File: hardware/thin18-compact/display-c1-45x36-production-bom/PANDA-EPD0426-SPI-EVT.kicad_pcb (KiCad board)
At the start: 2 copper layers, 45 x 36 mm, 37 parts, among them J1 DF40C-60DP-0.4V(51), J2 FH12-24S-0.5SH(55), Q1 NX3008NBK,215, U1 AIP74LVC2G17GC363.TR, U2 AIP74LVC2G17GC363.TR, U3 AIP74LVC2G17GC363.TR

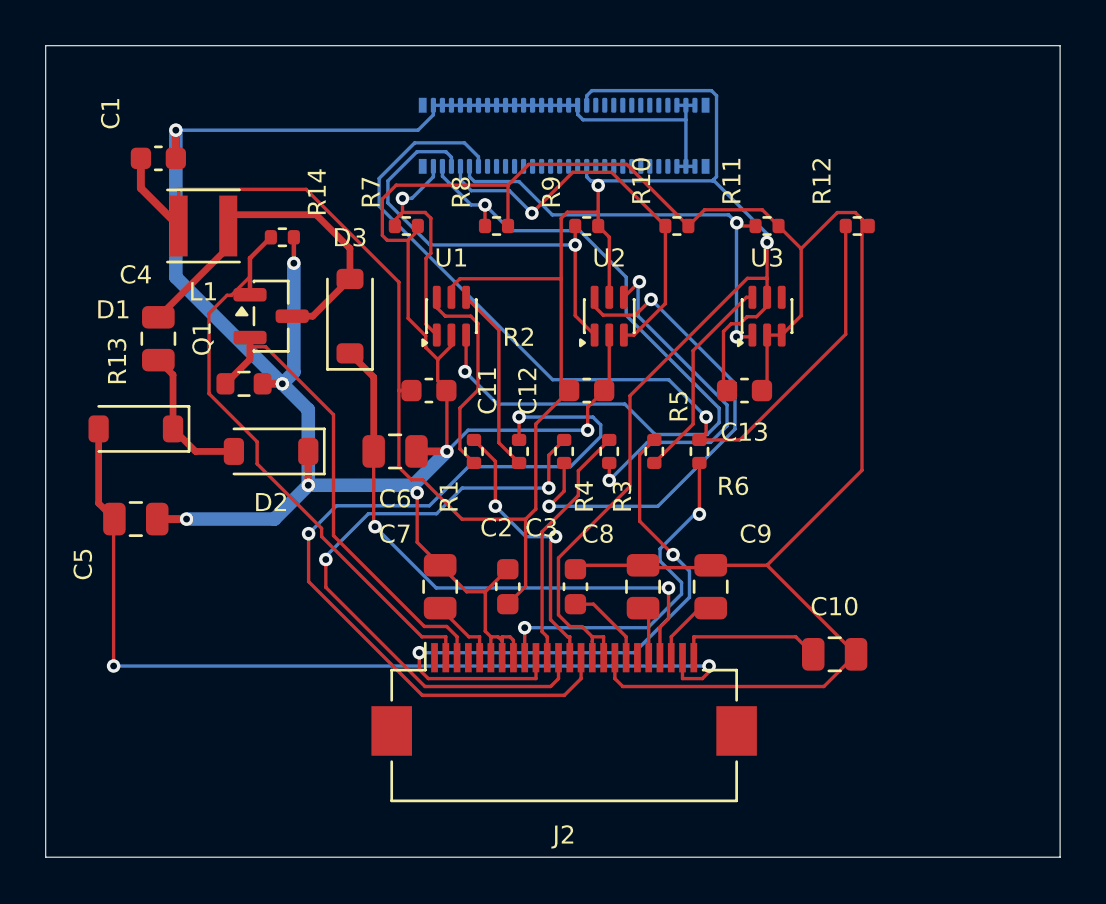
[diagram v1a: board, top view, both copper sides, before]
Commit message: hw: correct prototype footprints and prepare Split-C1 JLC CAM handoff
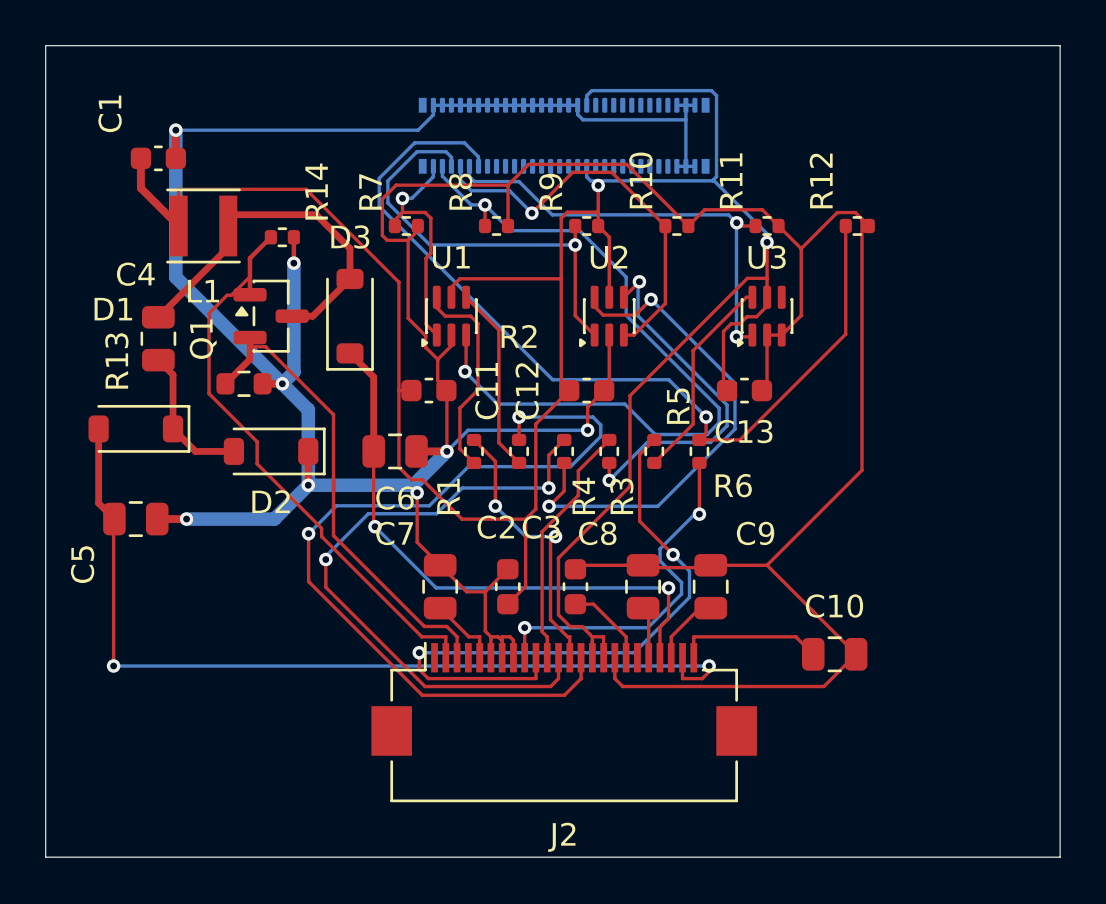
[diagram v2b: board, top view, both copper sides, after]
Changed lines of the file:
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@@
 			(effects
 				(font
-					(size 0.8 0.8)
-					(thickness 0.1)
+					(size 1 1)
+					(thickness 0.15)
 				)
 			)
@@
 			(effects
 				(font
-					(size 0.8 0.8)
-					(thickness 0.1)
+					(size 1 1)
+					(thickness 0.15)
 				)
 			)
@@
 			(effects
 				(font
-					(size 0.8 0.8)
-					(thickness 0.1)
+					(size 1 1)
+					(thickness 0.15)
 				)
 			)
@@
 			(effects
 				(font
-					(size 0.8 0.8)
-					(thickness 0.1)
+					(size 1 1)
+					(thickness 0.15)
 				)
 			)
@@
 			(effects
 				(font
-					(size 0.8 0.8)
-					(thickness 0.1)
+					(size 1 1)
+					(thickness 0.15)
 				)
 			)
@@
 			(effects
 				(font
-					(size 0.8 0.8)
-					(thickness 0.1)
+					(size 1 1)
+					(thickness 0.15)
 				)
 			)
@@
 			(effects
 				(font
-					(size 0.8 0.8)
-					(thickness 0.1)
+					(size 1 1)
+					(thickness 0.15)
 				)
 			)
@@
 			(effects
 				(font
-					(size 0.8 0.8)
-					(thickness 0.1)
+					(size 1 1)
+					(thickness 0.15)
 				)
 			)
@@
 			(effects
 				(font
-					(size 0.8 0.8)
-					(thickness 0.1)
+					(size 1 1)
+					(thickness 0.15)
 				)
 			)
@@
 			(effects
 				(font
-					(size 0.8 0.8)
-					(thickness 0.1)
+					(size 1 1)
+					(thickness 0.15)
 				)
 			)
@@
 			(effects
 				(font
-					(size 0.8 0.8)
-					(thickness 0.1)
+					(size 1 1)
+					(thickness 0.15)
 				)
 			)
@@
 			(effects
 				(font
-					(size 0.8 0.8)
-					(thickness 0.1)
+					(size 1 1)
+					(thickness 0.15)
 				)
 			)
@@
 			(effects
 				(font
-					(size 0.8 0.8)
-					(thickness 0.1)
+					(size 1 1)
+					(thickness 0.15)
 				)
 			)
@@
 			(effects
 				(font
-					(size 0.8 0.8)
-					(thickness 0.1)
+					(size 1 1)
+					(thickness 0.15)
 				)
 			)
@@
 			(effects
 				(font
-					(size 0.8 0.8)
-					(thickness 0.1)
+					(size 1 1)
+					(thickness 0.15)
 				)
 			)
@@
 			(effects
 				(font
-					(size 0.8 0.8)
-					(thickness 0.1)
+					(size 1 1)
+					(thickness 0.15)
 				)
 			)
@@
 			(effects
 				(font
-					(size 0.8 0.8)
-					(thickness 0.1)
+					(size 1 1)
+					(thickness 0.15)
 				)
 			)
@@
 			(effects
 				(font
-					(size 0.8 0.8)
-					(thickness 0.1)
+					(size 1 1)
+					(thickness 0.15)
 				)
 			)
@@
 			(effects
 				(font
-					(size 0.8 0.8)
-					(thickness 0.1)
+					(size 1 1)
+					(thickness 0.15)
 				)
 			)
@@
 			(effects
 				(font
-					(size 0.8 0.8)
-					(thickness 0.1)
+					(size 1 1)
+					(thickness 0.15)
 				)
 			)
@@
 			(effects
 				(font
-					(size 0.8 0.8)
-					(thickness 0.1)
+					(size 1 1)
+					(thickness 0.15)
 				)
 			)
@@
 			(effects
 				(font
-					(size 0.8 0.8)
-					(thickness 0.1)
+					(size 1 1)
+					(thickness 0.15)
 				)
 			)
@@
 			(effects
 				(font
-					(size 0.8 0.8)
-					(thickness 0.1)
+					(size 1 1)
+					(thickness 0.15)
 				)
 			)
@@
 			(effects
 				(font
-					(size 0.8 0.8)
-					(thickness 0.1)
+					(size 1 1)
+					(thickness 0.15)
 				)
 			)
@@
 			(effects
 				(font
-					(size 0.8 0.8)
-					(thickness 0.1)
+					(size 1 1)
+					(thickness 0.15)
 				)
 			)
@@
 			(effects
 				(font
-					(size 0.8 0.8)
-					(thickness 0.1)
+					(size 1 1)
+					(thickness 0.15)
 				)
 			)
@@
 			(effects
 				(font
-					(size 0.8 0.8)
-					(thickness 0.1)
+					(size 1 1)
+					(thickness 0.15)
 				)
 			)
@@
 			(effects
 				(font
-					(size 0.8 0.8)
-					(thickness 0.1)
+					(size 1 1)
+					(thickness 0.15)
 				)
 			)
@@
 			(effects
 				(font
-					(size 0.8 0.8)
-					(thickness 0.1)
+					(size 1 1)
+					(thickness 0.15)
 				)
 			)
@@
 			(effects
 				(font
-					(size 0.8 0.8)
-					(thickness 0.1)
+					(size 1 1)
+					(thickness 0.15)
 				)
 			)
@@
 			(effects
 				(font
-					(size 0.8 0.8)
-					(thickness 0.1)
+					(size 1 1)
+					(thickness 0.15)
 				)
 			)
@@
 			(effects
 				(font
-					(size 0.8 0.8)
-					(thickness 0.1)
+					(size 1 1)
+					(thickness 0.15)
 				)
 			)
@@
 			(effects
 				(font
-					(size 0.8 0.8)
-					(thickness 0.1)
+					(size 1 1)
+					(thickness 0.15)
 				)
 			)
@@
 			(effects
 				(font
-					(size 0.8 0.8)
-					(thickness 0.1)
+					(size 1 1)
+					(thickness 0.15)
 				)
 			)
@@
 			(effects
 				(font
-					(size 0.8 0.8)
-					(thickness 0.1)
+					(size 1 1)
+					(thickness 0.15)
 				)
 			)
@@
 			(effects
 				(font
-					(size 0.8 0.8)
-					(thickness 0.1)
+					(size 1 1)
+					(thickness 0.15)
 				)
 			)
@@
 			(effects
 				(font
-					(size 0.8 0.8)
-					(thickness 0.1)
+					(size 1 1)
+					(thickness 0.15)
 				)
 				(justify mirror)

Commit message: hw: apply reviewed domestic ECOs and gate incomplete Split-C1 orders
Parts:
- C4, C5, C6, C7, C8, C9: value 4.7u 25V X5R -> 4.7u 25V X7R
- D1, D2, D3: value MBR0530T1G -> MBR0530; footprint Diode_SMD:D_SOD-123 -> panda-r6-display:MBR0530_JSCJ_SOD123
- J1: value DF40C-60DP-0.4V(51) -> HC-PBB40C-60DP-0.4V-02; footprint Connector_Hirose_DF40:Hirose_DF40C-60DP-0.4V_2x30-1MP_P0.4mm -> panda-r6-display:HCTL_PBB40C_60DP_04V

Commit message: hw: apply domestic wire, FPC and inductor ECOs with replay guards
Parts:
- L1: value 47u 0.25A -> 47uH / Sunlord; footprint panda-r6-display:L_Taiyo_NRH3010_3030 -> panda-r6-display:Sunlord_SWPA3012_47u
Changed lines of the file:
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@@
 		)
 	)
-	(footprint "panda-r6-display:L_Taiyo_NRH3010_3030"
+	(footprint "panda-r6-display:Sunlord_SWPA3012_47u"
 		(layer "F.Cu")
 		(at 7 8)
-		(descr "Taiyo Yuden NRH3010 / LSXNE3030KK, 3.0x3.0mm maxH1.0mm. Catalog NR30 recommended land A0.8/Bcentre2.2/C2.7; supplier footprint review pending.")
+		(descr "Sunlord SWPA3012S manufacturer land pattern; original series drawing reviewed; Fab uses maximum body XY and no foreign 3D model.")
 		(property "Reference" "L1"
 			(at 0 2.924999 0)
@@
 			)
 		)
-		(property "Value" "47u 0.25A"
+		(property "Value" "47uH / Sunlord"
 			(at 0 2.4 0)
 			(layer "F.Fab")
@@
 			)
 		)
-		(property "Datasheet" "https://www.yuden.co.jp/"
-			(at 0 0 0)
-			(layer "F.Fab")
-			(hide yes)
-			(effects
-				(font
-					(size 1.27 1.27)
-				)
-			)
-		)(property "Manufacturer" "Taiyo Yuden" (at 0 0 0) (layer "F.Fab") (hide yes) (effects (font (size 1 1))))
-		(property "Description" ""
+		(property "Datasheet" "https://atta.szlcsc.com/upload/public/pdf/source/20241120/5FB31A17AAA509171003FB8365AF70A5.pdf"
 			(at 0 0 0)
 			(layer "F.Fab")
@@
 			)
 		)
-		(property "MPN" "LSXNE3030KKT470MN"
+(property "LCSC" ""
+			(at 0 0 0)
+			(layer "F.Fab")
+			(hide yes)
+			(effects
+				(font
+					(size 1.27 1.27)
+				)
+			)
+		)(property "Manufacturer" "Sunlord" (at 0 0 0) (layer "F.Fab") (hide yes) (effects (font (size 1 1))))
+		(property "Description" "47uH +/-20%,DCR1.885ohm max,Isat(Max/Typ).27/.35A,Irms(Max/Typ).35/.40A from original2024-06-19 p5; current headings retained, not claimed as guaranteed minimum. Body3.0+/-0.2mm square,max height1.2mm. p2 lands0.8x2.7mm,inner gap1.5mm,centers+/-1.15mm. Original maxDCR2.46ohm,height1.0mm,current.25A; boost peak/RESE corners, ripple, thermal and efficiency remain EVT. Taller by.2mm, mechanical budget updated. Exact supply/packing not yet accepted."
+			(at 0 0 0)
+			(layer "F.Fab")
+			(hide yes)
+			(effects
+				(font
+					(size 1.27 1.27)
+				)
+			)
+		)
+		(property "MPN" "SWPA3012S470MT"
 			(at 0 0 0)
 			(layer "F.SilkS")
@@
 		(attr smd)
 		(duplicate_pad_numbers_are_jumpers no)
-		(fp_line
-			(start -1.6 -1.6)
-			(end 1.6 -1.6)
-			(stroke
-				(width 0.12)
-				(type default)
-			)
-			(layer "F.SilkS")
-		)
-		(fp_line
-			(start -1.6 1.6)
-			(end 1.6 1.6)
-			(stroke
-				(width 0.12)
-				(type default)
-			)
-			(layer "F.SilkS")
-		)
-		(fp_rect
-			(start -1.8 -1.8)
-			(end 1.8 1.8)
-			(stroke
-				(width 0.05)
-				(type default)
-			)
-			(fill no)
-			(layer "F.CrtYd")
-		)
-		(fp_rect
-			(start -1.5 -1.5)
-			(end 1.5 1.5)
-			(stroke
-				(width 0.1)
-				(type default)
-			)
-			(fill no)
-			(layer "F.Fab")
-		)
 		(pad "1" smd rect
-			(at -1.1 0)
+			(at -1.15 0)
 			(size 0.8 2.7)
 			(layers "F.Cu" "F.Mask" "F.Paste")
@@
 		)
 		(pad "2" smd rect
-			(at 1.1 0)
+			(at 1.15 0)
 			(size 0.8 2.7)
 			(layers "F.Cu" "F.Mask" "F.Paste")
@@
 		)
 		(embedded_fonts no)
-	)
+(fp_rect (start -1.6 -1.6) (end 1.6 1.6) (stroke (width 0.1) (type solid)) (fill no) (layer "F.Fab"))
+(fp_rect (start -1.85 -1.85) (end 1.85 1.85) (stroke (width 0.05) (type solid)) (fill no) (layer "F.CrtYd"))
+)
 	(footprint "Capacitor_SMD:C_0805_2012Metric"
 		(layer "F.Cu")

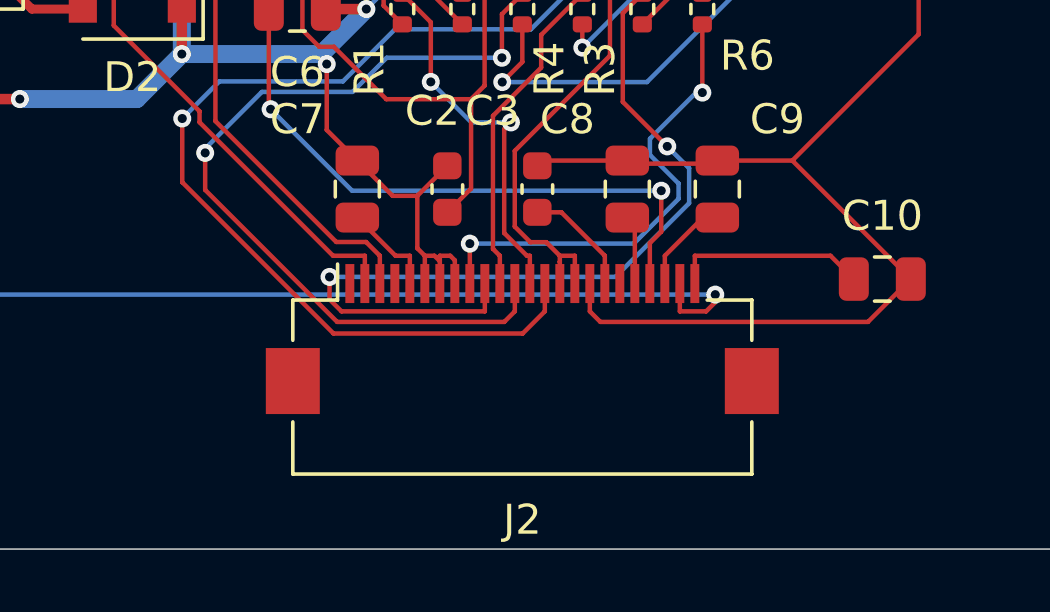
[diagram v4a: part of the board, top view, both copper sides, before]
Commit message: hardware: close three imported Split-C1 refs and two SMT maps
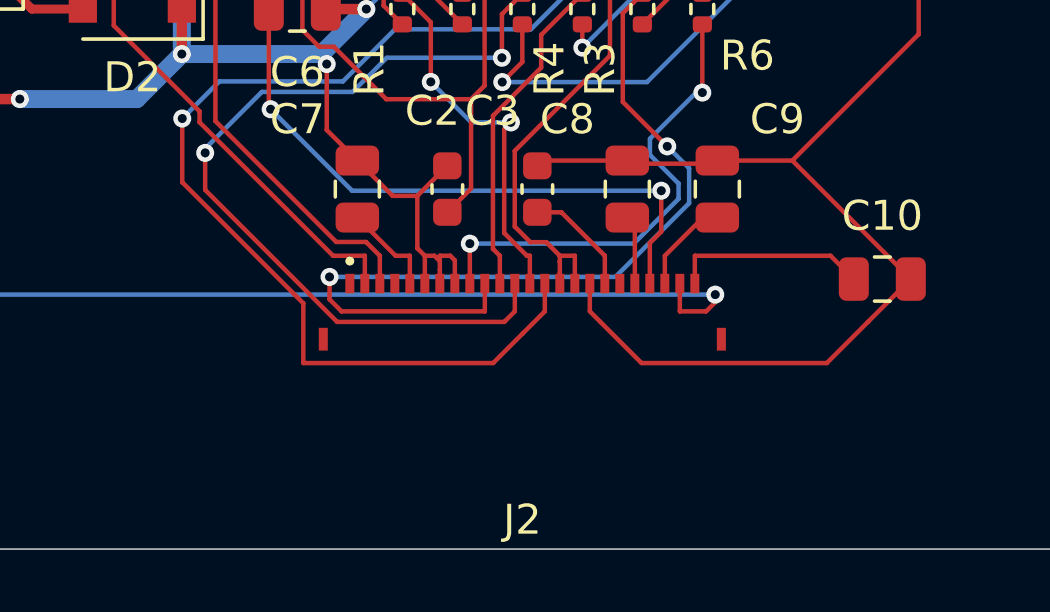
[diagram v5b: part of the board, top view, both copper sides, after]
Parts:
- J2: value FH12-24S-0.5SH(55) -> X05A10L24G; footprint Connector_FFC-FPC:Hirose_FH12-24S-0.5SH_1x24-1MP_P0.50mm_Horizontal -> panda-r6-display:XKB_X05A10L24G
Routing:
- net /MOSI: track 37.6 -> 39.6 mm
- net /GND: track 190.5 -> 191.6 mm

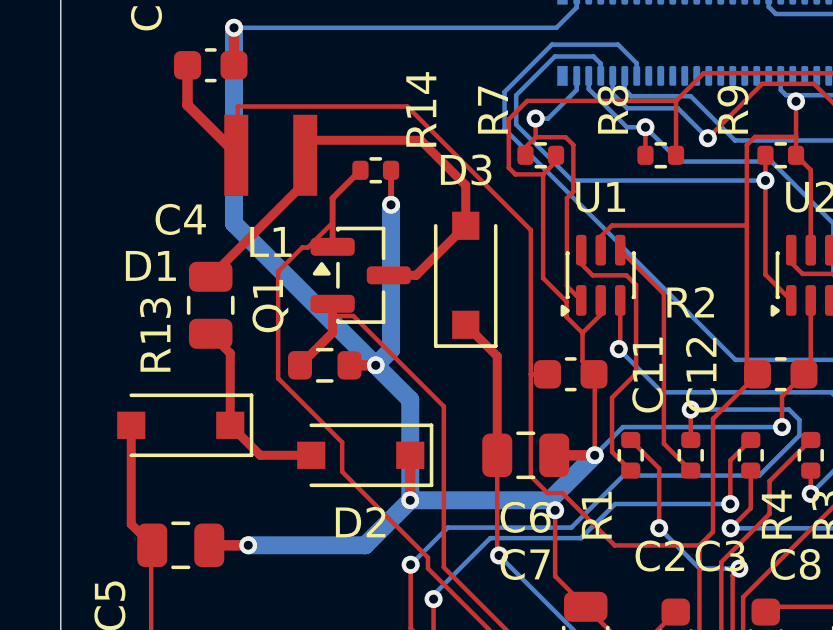
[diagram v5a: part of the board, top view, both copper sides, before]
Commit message: hw: complete Split-C1 domestic RTC backup and EPD MOS ECO
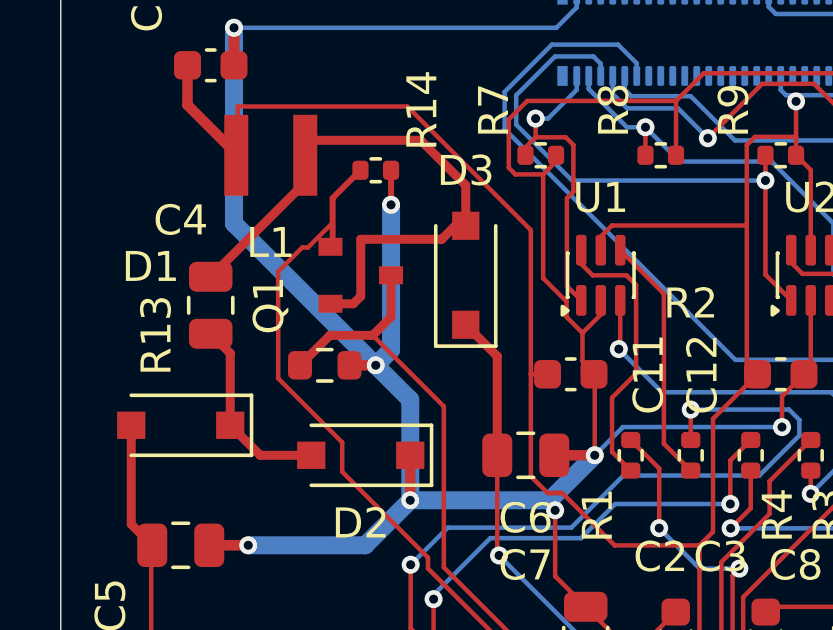
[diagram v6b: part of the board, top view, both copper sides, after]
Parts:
- Q1: value NX3008NBK,215 -> NX3008NBK,215-JSM; footprint Package_TO_SOT_SMD:SOT-23 -> panda-r6-display:JSM_NX3008NBK_SOT23
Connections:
- Q1 pad 2: /RESE -> /BOOST_SW
- Q1 pad 3: /BOOST_SW -> /RESE
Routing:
- net /BOOST_SW: track 16.5 -> 19.9 mm
- net /RESE: track 21.1 -> 22.1 mm
